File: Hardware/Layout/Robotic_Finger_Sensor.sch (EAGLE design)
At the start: 11 parts, among them U1 VCNL4040

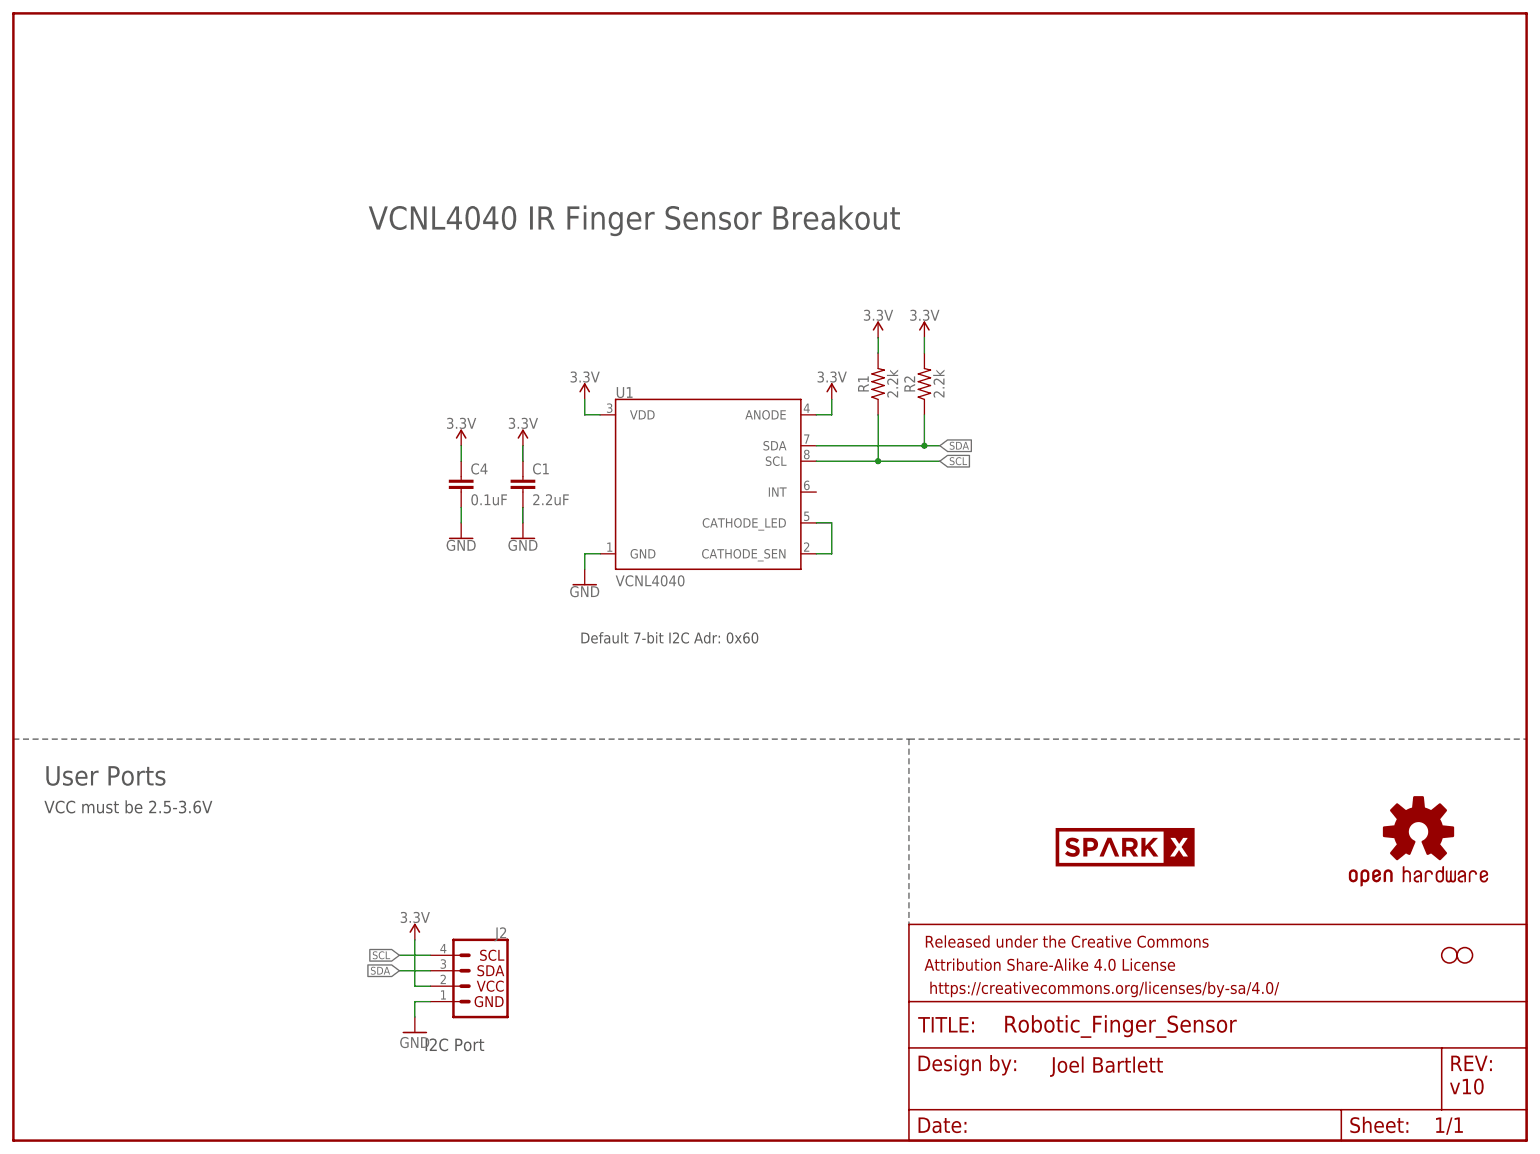
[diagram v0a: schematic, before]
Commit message: Adding PDF schematic
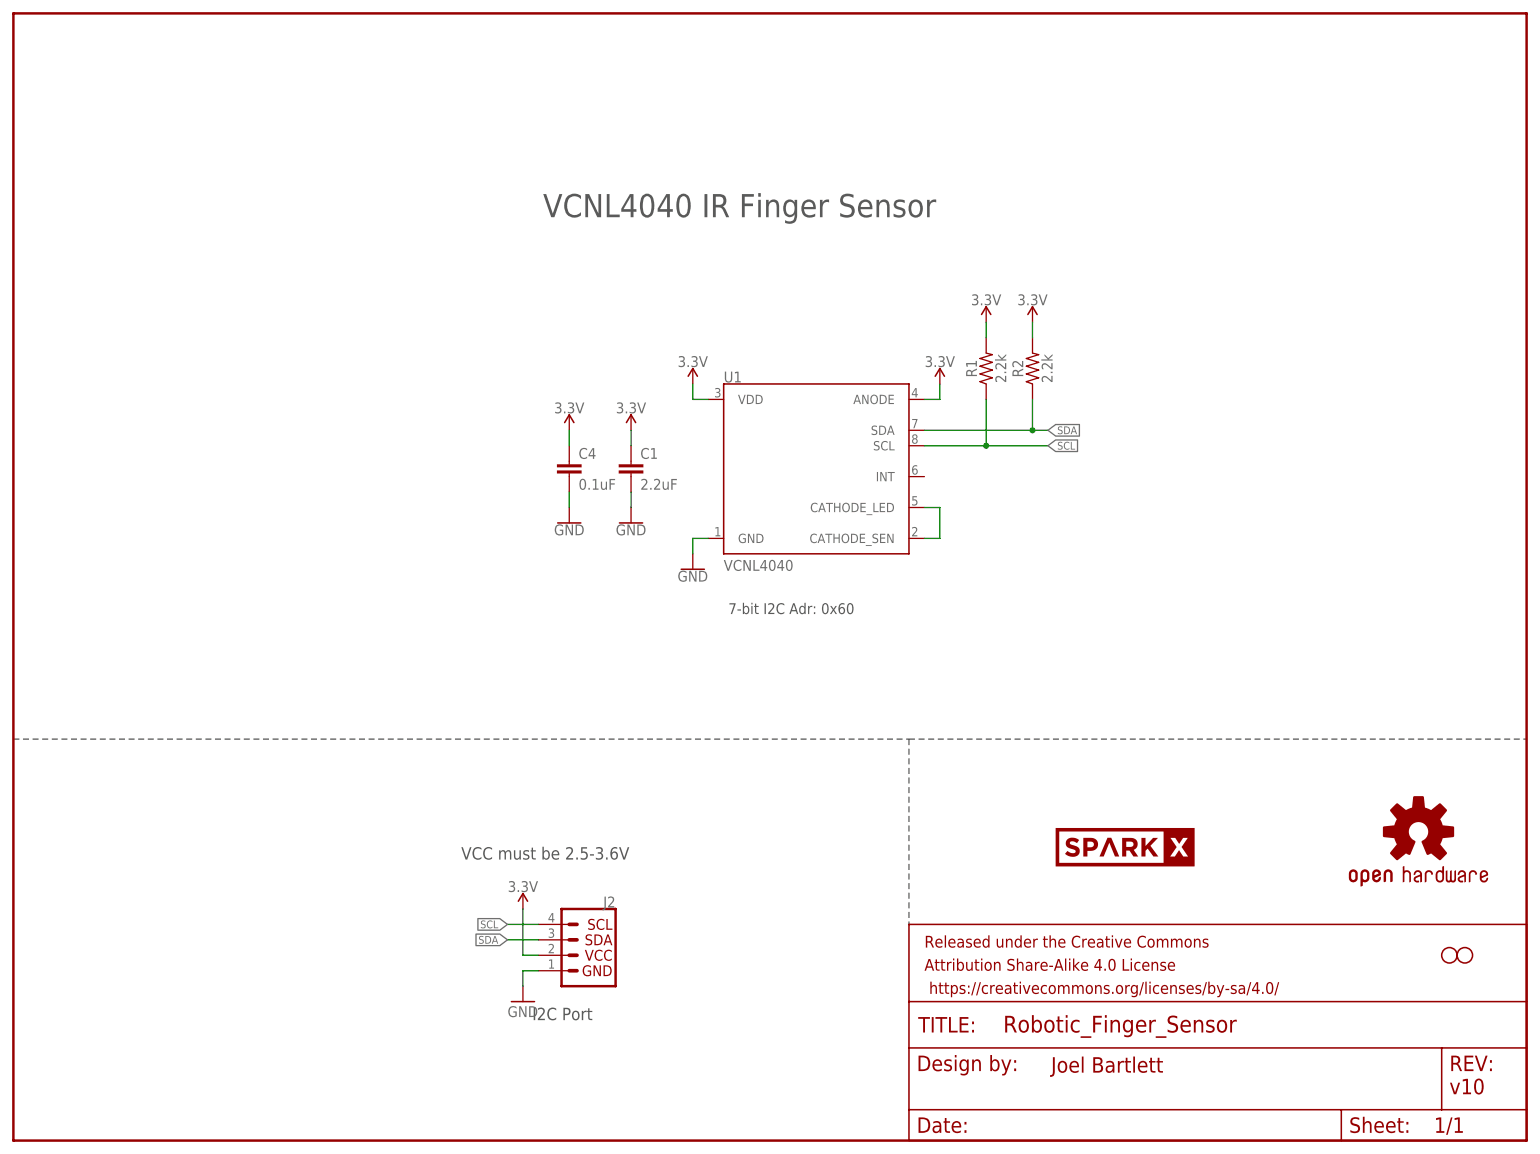
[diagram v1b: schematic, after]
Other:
- note added: "7-bit I2C Adr: 0x60"
- note added: "VCNL4040 IR Finger Sensor"
- note removed: "Default 7-bit I2C Adr: 0x60"
- note removed: "User Ports"
- note removed: "VCNL4040 IR Finger Sensor Breakout"
- moved on the sheet: C1, C4, J2, R1, R2, U1

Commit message: Adding pressure sensor. Cleaning up repo.
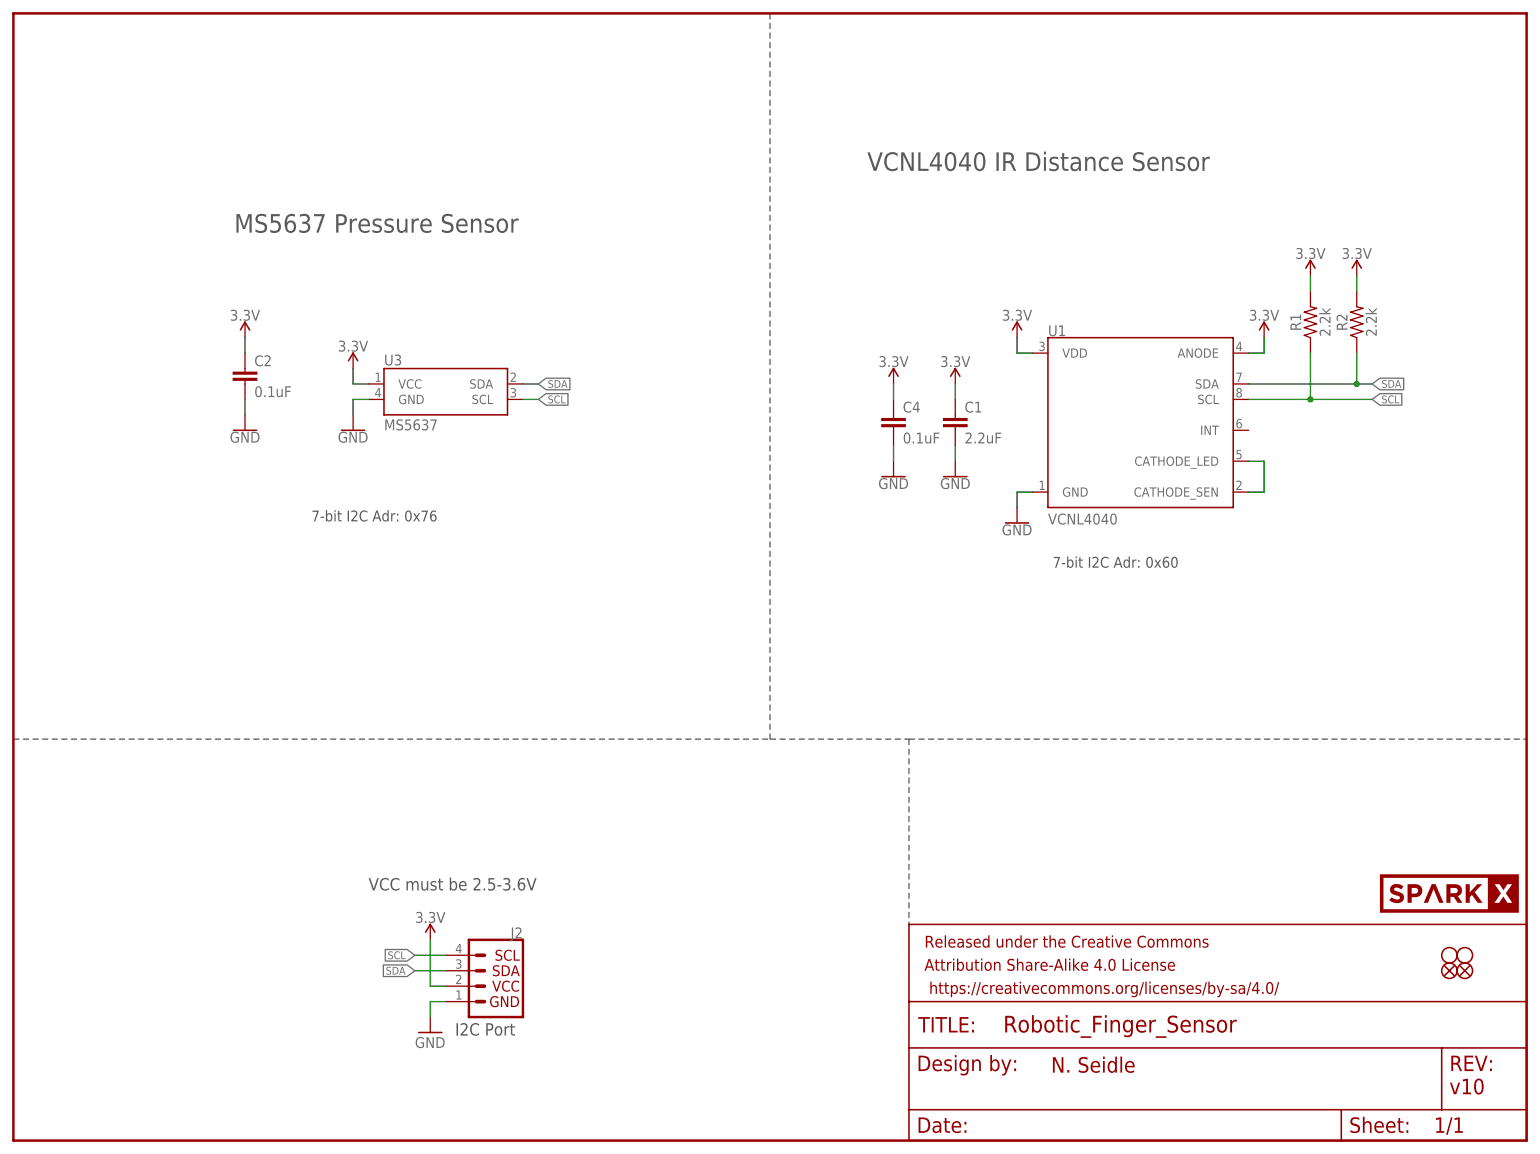
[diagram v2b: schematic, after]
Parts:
- removed U$1: OSHW-LOGOS, SparkFun:OSHW-LOGOS
- added C2: 0.1uF, SparkFun-Capacitors:0.1UF-0603-25V-(+80/-20%)
- added FD1, FD2: FIDUCIALUFIDUCIAL, SparkFun-Aesthetics:FIDUCIALUFIDUCIAL
- added U3: MS5637, MS5637:MS5637
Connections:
- net 3.3V: now also C2.1, U3.VCC
- net GND: now also C2.2, U3.GND
- net SCL: now also U3.SCL
- net SDA: now also U3.SDA
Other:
- note added: "7-bit I2C Adr: 0x76"
- note added: "MS5637 Pressure Sensor"
- note added: "N. Seidle"
- note added: "VCNL4040 IR Distance Sensor"
- note removed: "Joel Bartlett"
- note removed: "VCNL4040 IR Finger Sensor"
- moved on the sheet: C1, C4, J2, R1, R2, U1
